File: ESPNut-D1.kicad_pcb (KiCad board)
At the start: 2 copper layers, 44 x 20 mm, 77 parts, among them J1 USB_C_Receptacle_USB2.0, J2 ESP_CONN, J3 USB_PADS, J4 ESP_PROG, Q1 BC817, Q2 BC817, Q3 Si2302CDS, SW1 ESP_RST, SW2 ESP_BOOT, SW3 ESP_VDD_SW, SW4 POW_CTRL, U1 CH340G, U2 MIC5219-3.3YM5, Y1 12MHz

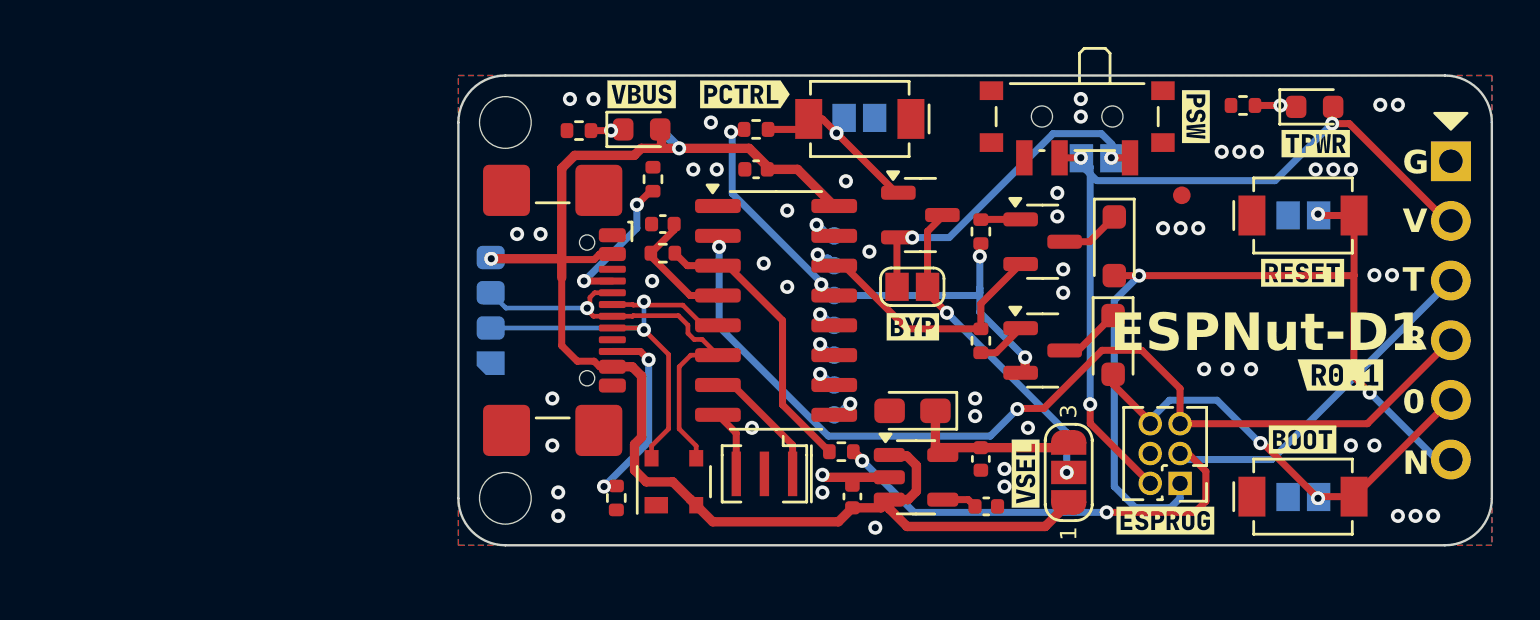
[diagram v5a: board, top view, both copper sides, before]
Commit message: New Revision `R0.2`
- Schematic
  - Deleted the Mosfet based power control circuit.
    - Replaced it with `AP22804AW5` based circuit.
    - Not because it is not working, but because a proper load switch is more reliable.
  - Added 6-pin `SM06B-SRSS-TB` JST-SH connector for target ESP.
    - The THT pin-headers will be changes to SMD one and placed on the back side.
  - Added `PCM12SMTR` SPDT switch for ESP voltage selection.
    - Removed the 3-pin solder jumper.
- PCB
  - Imported all changes to the PCB.
  - Deleted all existing tracks and vias.
  - Rearranged the components.
  - Updated label styles and placements.
  - There is now more alignment and symmetry.
  - Routing pending.
- New Revision `R0.2`.
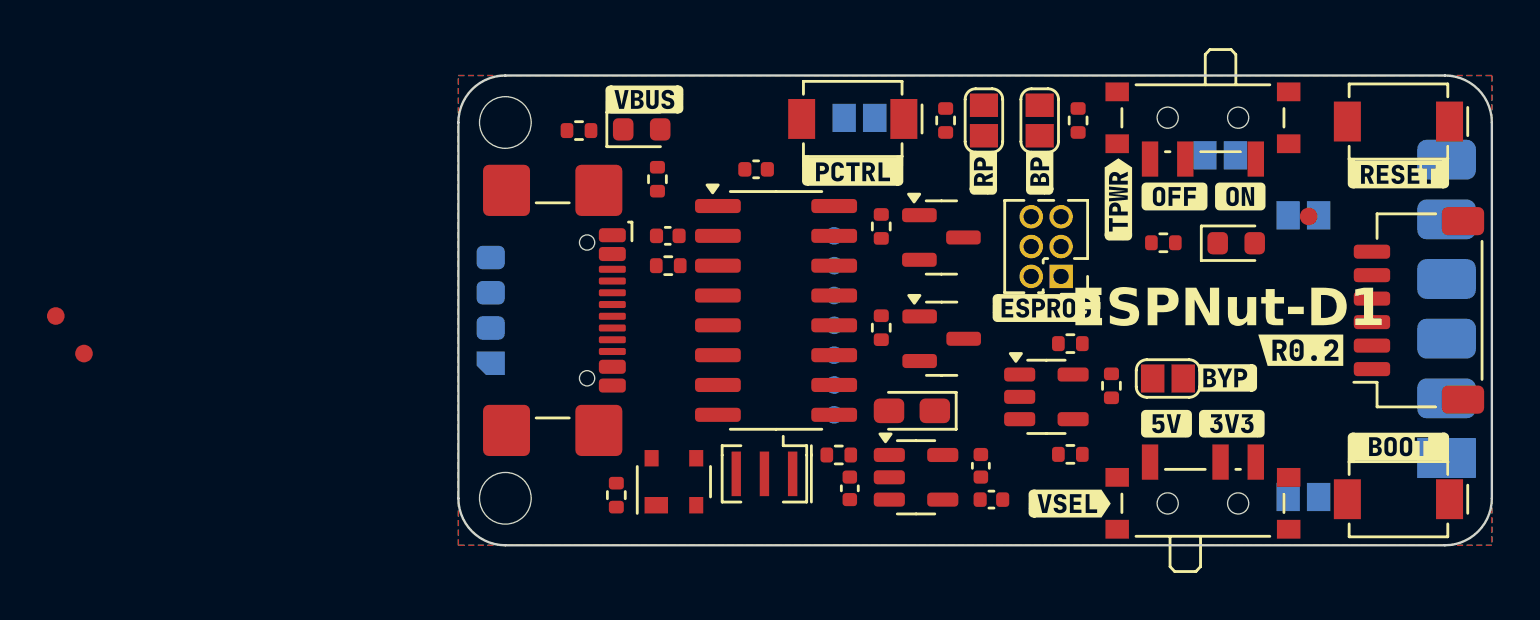
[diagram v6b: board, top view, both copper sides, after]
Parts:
- removed the D1 at (146.9, 77.3)
- removed D4: RB751V40, Diode_SMD:D_SOD-323_HandSoldering
- removed D5: ESP_PWR, LED_SMD:LED_0603_1608Metric
- removed the JP3 at (138.3, 79.0)
- removed the JP4 at (145.0, 86.9)
- removed Q3: Si2302CDS, Package_TO_SOT_SMD:SOT-23
- removed the R8 at (131.7, 72.3)
- removed the R9 at (152.4, 71.3)
- removed the kibuzzard-67F0B0FE at (150.4, 71.8)
- removed kibuzzard-67F0B12D: G***, kibuzzard-67F0B12D
- removed kibuzzard-67F0B13A: G***, kibuzzard-67F0B13A
- removed the kibuzzard-67F0B154 at (154.9, 85.5)
- removed the kibuzzard-67F0B15A at (154.9, 78.4)
- removed the kibuzzard-67F0B186 at (155.5, 72.9)
- removed kibuzzard-67F0B314: G***, kibuzzard-67F0B314
- removed the kibuzzard-67F0B847 at (156.6, 82.8)
- added D3: ESP_PWR, LED_SMD:LED_0603_1608Metric, F.Cu at (152.1, 77.1)
- added J3: ESP_CONN, CSE_Connector_JST_SH:JST_SH_SM06B-SRSS-TB_1x06-1MP_P1.00mm_Horizontal, F.Cu at (159.9, 80.0)
- added JP1: RST_PUE, CSE_Solder-Jumper:Solder-Jumper-1x2_P1.3mm_Open_Rounded_1.0x1.2mm, F.Cu at (141.4, 71.9)
- added JP2: BT_PUE, CSE_Solder-Jumper:Solder-Jumper-1x2_P1.3mm_Open_Rounded_1.0x1.2mm, F.Cu at (143.8, 71.9)
- added JP6: ESP_VDD_SW, CSE_Solder-Jumper:Solder-Jumper-1x2_P1.3mm_Open_Rounded_1.0x1.2mm, B.Cu at (151.4, 73.4)
- added R10: 10K, Resistor_SMD:R_0402_1005Metric, F.Cu at (146.8, 83.2)
- added R11: 220R, Resistor_SMD:R_0402_1005Metric, F.Cu at (145.1, 86.1)
- added R12: 10K, Resistor_SMD:R_0402_1005Metric, F.Cu at (145.1, 81.4)
- added R13: 220R, Resistor_SMD:R_0402_1005Metric, F.Cu at (149.0, 77.1)
- added R3: 10K, Resistor_SMD:R_0402_1005Metric, F.Cu at (139.7, 71.9)
- added R4: 10K, Resistor_SMD:R_0402_1005Metric, F.Cu at (145.4, 71.9)
- added SW4: ESPV_SEL, Button_Switch_SMD:SW_SPDT_PCM12, F.Cu at (150.7, 87.9)
- added U3: AP22804AW5, Package_TO_SOT_SMD:SOT-23-5, F.Cu at (144.0, 83.7)
- added kibuzzard-6882689F: G***, kibuzzard-6882689F, F.Cu at (152.3, 75.2)
- added kibuzzard-688268B9: G***, kibuzzard-688268B9, F.Cu at (149.5, 75.2)
- added kibuzzard-688268E7: G***, kibuzzard-688268E7, F.Cu at (154.9, 81.7)
- added kibuzzard-68826928: G***, kibuzzard-68826928, F.Cu at (151.9, 84.8)
- added kibuzzard-68826931: G***, kibuzzard-68826931, F.Cu at (149.1, 84.8)
- added kibuzzard-688269BA: G***, kibuzzard-688269BA, F.Cu at (151.7, 82.9)
- added kibuzzard-688269D8: G***, kibuzzard-688269D8, F.Cu at (145.1, 88.2)
- added kibuzzard-68826DC1: G***, kibuzzard-68826DC1, F.Cu at (147.1, 75.2)
- added kibuzzard-688272B9: G***, kibuzzard-688272B9, F.Cu at (143.8, 74.0)
- added kibuzzard-688272CF: G***, kibuzzard-688272CF, F.Cu at (141.3, 74.0)
- added kibuzzard-688273BB: G***, kibuzzard-688273BB, F.Cu at (159.0, 85.8)
- added kibuzzard-68827414: G***, kibuzzard-68827414, F.Cu at (159.0, 74.2)
- added kibuzzard-68827490: G***, kibuzzard-68827490, F.Cu at (135.8, 74.1)
- J2: footprint Connector_PinHeader_2.54mm:PinHeader_1x06_P2.54mm_Vertical -> CSE_Solderpads:Solderpad_1x06_P2.54mm_Rounded_Rectangle; moved to B.Cu
- JP5: value ESP_VDD_SW -> VDD_CTRL_BYP; moved to F.Cu
- TP10, TP11: moved to F.Cu
- moved TP10 55.1 mm to (101.9, 80.2)
- moved TP11 52.6 mm to (103.1, 81.8)
- moved kibuzzard-67F0B829 10.4 mm to (144.0, 79.9)
- moved J5 10.2 mm to (144.7, 78.6)
- moved JP5 9.85 mm to (149.2, 82.9)
- moved J2 6.29 mm to (161.1, 79.9)
- moved SW1 5.70 mm to (159.0, 72.0), turned to 180 degrees
- moved FD1 5.47 mm to (155.2, 76.0)
- moved SW3 5.35 mm to (150.7, 72.1)
- moved Q2 4.33 mm to (139.6, 81.2)
- moved Q1 4.31 mm to (139.6, 76.9)
- moved R9 4.28 mm to (137.0, 80.7)
- moved R6 4.25 mm to (137.0, 76.4)
- moved SW2 4.07 mm to (159.0, 88.0), turned to 180 degrees
- moved R8 0.58 mm to (127.9, 78.1)
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- renumbered D2 to D1, D3 to D2, J3 to J4, J4 to J5, JP1 to JP3, JP2 to JP4, JP6 to JP7, R3 to R5, R4 to R6, R5 to R7, R6 to R8, R7 to R9, SW4 to SW5, TP8 to TP1, TP9 to TP2, TP1 to TP3, TP2 to TP4, TP3 to TP5, TP4 to TP6, TP5 to TP7, TP6 to TP8, TP7 to TP9
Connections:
- JP5 pad 1: /ESP_VDD_O -> Net-(JP5-A)
- JP5 pad 2: Net-(JP3-A) -> /ESP_VDD_I
- Q1 pad 3: Net-(D1-K) (its old number) -> /ESP_NRST
- Q2 pad 3: Net-(D4-K) -> /ESP_IO0
- SW3 pad 1: Net-(JP3-A) -> Net-(JP5-A)
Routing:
- net VBUS: track 61.7 -> 0.00 mm, vias 2 -> 0
- net /ESP_RX0: track 42.1 -> 0.00 mm, vias 2 -> 0
- net /ESP_NRST: track 37.6 -> 0.00 mm, vias 3 -> 0
- net /ESP_VDD_O: track 36.5 -> 0.00 mm, vias 3 -> 0
- net /ESP_TX0: track 33.8 -> 0.00 mm, vias 2 -> 0
- net /DTR: track 22.3 -> 0.00 mm, vias 4 -> 0
- net /USB_D+: track 20.2 -> 0.00 mm, vias 2 -> 0
- net /ESP_IO0: track 19.5 -> 0.00 mm, vias 2 -> 0
- net /USB_D-: track 18.5 -> 0.00 mm, vias 1 -> 0
- net Net-(JP3-A): track 14.7 -> 0.00 mm, vias 2 -> 0
- net /ESP_VDD_I: track 13.7 -> 0.00 mm, vias 2 -> 0
- net /RTS: track 12.7 -> 0.00 mm, vias 1 -> 0
- net Net-(U1-RXD): track 12.2 -> 0.00 mm
- net Net-(J1-CC2): track 8.41 -> 0.00 mm, vias 2 -> 0
- net +3V3: track 7.79 -> 0.00 mm
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
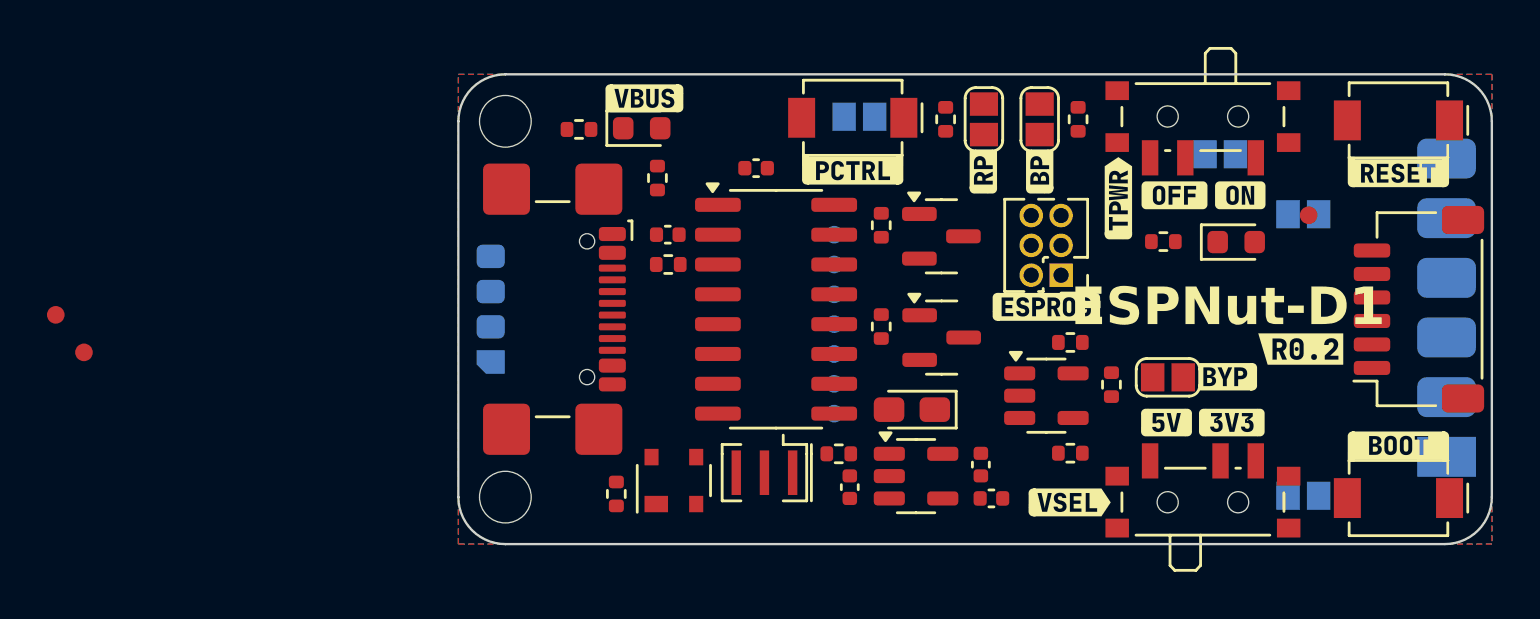
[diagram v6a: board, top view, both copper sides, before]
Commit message: Routing completed
- Schematic
  - Updated BoM.
  - Reset the annotations.
- PCB
  - Imported all changes to the PCB.
  - Routing completed.
  - DRC passes.
  - Updated Fab layers.
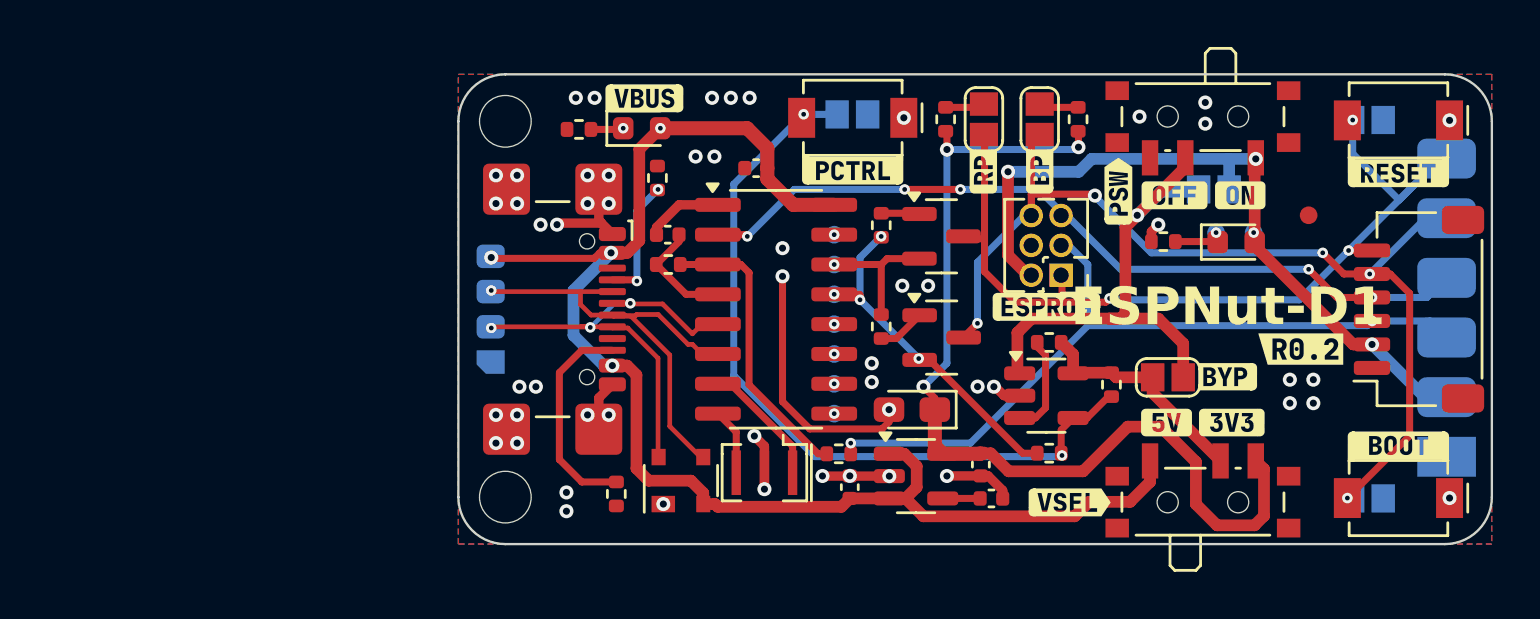
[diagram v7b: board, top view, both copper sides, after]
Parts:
- removed kibuzzard-67F0B15A: G***, kibuzzard-67F0B15A
- removed kibuzzard-67F0B186: G***, kibuzzard-67F0B186
- removed kibuzzard-67F0B847: G***, kibuzzard-67F0B847
- removed kibuzzard-68826DC1: G***, kibuzzard-68826DC1
- added kibuzzard-68837A0C: G***, kibuzzard-68837A0C, B.Cu at (154.7, 71.9)
- added kibuzzard-68837ACD: G***, kibuzzard-68837ACD, B.Cu at (152.0, 78.1)
- added kibuzzard-68837FCA: G***, kibuzzard-68837FCA, F.Cu at (147.1, 74.9)
- added kibuzzard-6883846F: G***, kibuzzard-6883846F, B.Cu at (125.8, 88.5)
- TP1: value CTS -> VBUS
- TP10: value CTS -> ESP_VDD_O; moved to B.Cu
- TP11: value CTS -> ESP_PWR_1; moved to B.Cu
- TP2: value CTS -> VBUS_LED_1
- moved TP10 51.1 mm to (152.9, 76.7)
- moved TP11 48.5 mm to (151.3, 76.7)
- moved G*** 15.4 mm to (128.2, 81.8)
- moved JP3 4.86 mm to (157.7, 71.9), turned to 180 degrees
- moved kibuzzard-67F0C2BD 3.79 mm to (132.7, 71.7)
- moved JP4 2.75 mm to (157.7, 88.1), turned to 180 degrees
- moved kibuzzard-67F0B0FE 2.51 mm to (148.7, 74.9)
- moved kibuzzard-67F0B154 1.72 mm to (155.0, 88.1)
- moved JP6 1.52 mm to (151.2, 74.9), turned to 180 degrees
- moved R11 0.90 mm to (144.2, 86.1)
- moved R12 0.90 mm to (144.2, 81.4)
- moved JP7 0.32 mm to (135.8, 71.7)
- moved D2 0.30 mm to (128.5, 87.3)
- turned JP5 to 180 degrees
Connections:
- SW3 pad 1: Net-(JP5-A) -> /ESP_VDD_O
- SW3 pad 2: /ESP_VDD_O -> Net-(JP5-A)
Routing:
- net VBUS: track 0.00 -> 60.6 mm, vias 0 -> 4
- net /ESP_IO0: track 0.00 -> 43.0 mm, vias 0 -> 5
- net +3V3: track 0.00 -> 41.1 mm, vias 0 -> 3
- net /ESP_NRST: track 0.00 -> 38.5 mm, vias 0 -> 3
- net /ESP_RX0: track 0.00 -> 34.2 mm, vias 0 -> 5
- net Net-(JP7-B): track 0.00 -> 32.9 mm, vias 0 -> 2
- net /ESP_TX0: track 0.00 -> 32.3 mm, vias 0 -> 2
- net /ESP_VDD_O: track 0.00 -> 31.6 mm, vias 0 -> 4
- net GND: track 0.00 -> 30.9 mm, vias 0 -> 54
- net Net-(JP5-A): track 0.00 -> 22.5 mm, vias 0 -> 1
- net /USB_D-: track 0.00 -> 20.6 mm, vias 0 -> 1
- net /USB_D+: track 0.00 -> 19.7 mm, vias 0 -> 3
- net /DTR: track 0.00 -> 14.6 mm, vias 0 -> 4
- net Net-(U1-RXD): track 0.00 -> 12.4 mm
- net /ESP_VDD_I: track 0.00 -> 9.76 mm
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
